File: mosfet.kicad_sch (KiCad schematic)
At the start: 4 parts

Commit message: v1
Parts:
- gave numbers to parts that had none: 4
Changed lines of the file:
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@@
 		(dnp no)
 		(fields_autoplaced yes)
-		(property "Reference" "#PWR032"
+		(property "Reference" "#PWR043"
 			(at 157.48 90.17 0)
 			(effects
@@
 			(project "aroma"
 				(path "/41d97073-34b5-4be3-afd3-c3d0ba6d78a9/41dcc568-047e-40c3-8917-993a0c1d8777"
-					(reference "#PWR042")
+					(reference "#PWR047")
 					(unit 1)
 				)
 				(path "/41d97073-34b5-4be3-afd3-c3d0ba6d78a9/5284dedf-81b9-4455-a1ae-4e68003b13db"
-					(reference "#PWR019")
+					(reference "#PWR045")
 					(unit 1)
 				)
 				(path "/41d97073-34b5-4be3-afd3-c3d0ba6d78a9/5e97d013-66fe-470c-accb-01dc7cf23fc6"
-					(reference "#PWR044")
+					(reference "#PWR049")
 					(unit 1)
 				)
 				(path "/41d97073-34b5-4be3-afd3-c3d0ba6d78a9/8980739a-e055-493d-bd80-b94c801de5e3"
-					(reference "#PWR032")
+					(reference "#PWR043")
 					(unit 1)
 				)
 				(path "/41d97073-34b5-4be3-afd3-c3d0ba6d78a9/b2304c8e-7f55-47b7-996b-0a7058ef6c5d"
-					(reference "#PWR049")
+					(reference "#PWR053")
 					(unit 1)
 				)
 				(path "/41d97073-34b5-4be3-afd3-c3d0ba6d78a9/fe386d5b-d6d2-4631-9499-27522be29692"
-					(reference "#PWR046")
+					(reference "#PWR051")
 					(unit 1)
 				)
@@
 		(dnp no)
 		(fields_autoplaced yes)
-		(property "Reference" "U?"
+		(property "Reference" "U8"
 			(at 134.62 90.17 0)
 			(effects
@@
 			(project "aroma"
 				(path "/41d97073-34b5-4be3-afd3-c3d0ba6d78a9/41dcc568-047e-40c3-8917-993a0c1d8777"
-					(reference "U?")
+					(reference "U10")
 					(unit 1)
 				)
 				(path "/41d97073-34b5-4be3-afd3-c3d0ba6d78a9/5284dedf-81b9-4455-a1ae-4e68003b13db"
-					(reference "U?")
+					(reference "U9")
 					(unit 1)
 				)
 				(path "/41d97073-34b5-4be3-afd3-c3d0ba6d78a9/5e97d013-66fe-470c-accb-01dc7cf23fc6"
-					(reference "U?")
+					(reference "U11")
 					(unit 1)
 				)
 				(path "/41d97073-34b5-4be3-afd3-c3d0ba6d78a9/8980739a-e055-493d-bd80-b94c801de5e3"
-					(reference "U?")
+					(reference "U8")
 					(unit 1)
 				)
 				(path "/41d97073-34b5-4be3-afd3-c3d0ba6d78a9/b2304c8e-7f55-47b7-996b-0a7058ef6c5d"
-					(reference "U?")
+					(reference "U13")
 					(unit 1)
 				)
 				(path "/41d97073-34b5-4be3-afd3-c3d0ba6d78a9/fe386d5b-d6d2-4631-9499-27522be29692"
-					(reference "U?")
+					(reference "U12")
 					(unit 1)
 				)
@@
 		(dnp no)
 		(fields_autoplaced yes)
-		(property "Reference" "R?"
+		(property "Reference" "R21"
 			(at 113.03 106.6799 0)
 			(effects
@@
 			(project "aroma"
 				(path "/41d97073-34b5-4be3-afd3-c3d0ba6d78a9/41dcc568-047e-40c3-8917-993a0c1d8777"
-					(reference "R?")
+					(reference "R23")
 					(unit 1)
 				)
 				(path "/41d97073-34b5-4be3-afd3-c3d0ba6d78a9/5284dedf-81b9-4455-a1ae-4e68003b13db"
-					(reference "R?")
+					(reference "R22")
 					(unit 1)
 				)
 				(path "/41d97073-34b5-4be3-afd3-c3d0ba6d78a9/5e97d013-66fe-470c-accb-01dc7cf23fc6"
-					(reference "R?")
+					(reference "R24")
 					(unit 1)
 				)
 				(path "/41d97073-34b5-4be3-afd3-c3d0ba6d78a9/8980739a-e055-493d-bd80-b94c801de5e3"
-					(reference "R?")
+					(reference "R21")
 					(unit 1)
 				)
 				(path "/41d97073-34b5-4be3-afd3-c3d0ba6d78a9/b2304c8e-7f55-47b7-996b-0a7058ef6c5d"
-					(reference "R?")
+					(reference "R26")
 					(unit 1)
 				)
 				(path "/41d97073-34b5-4be3-afd3-c3d0ba6d78a9/fe386d5b-d6d2-4631-9499-27522be29692"
-					(reference "R?")
+					(reference "R25")
 					(unit 1)
 				)
@@
 		(dnp no)
 		(fields_autoplaced yes)
-		(property "Reference" "J?"
+		(property "Reference" "J5"
 			(at 184.15 93.9799 0)
 			(effects
@@
 			(project "aroma"
 				(path "/41d97073-34b5-4be3-afd3-c3d0ba6d78a9/41dcc568-047e-40c3-8917-993a0c1d8777"
-					(reference "J?")
+					(reference "J7")
 					(unit 1)
 				)
 				(path "/41d97073-34b5-4be3-afd3-c3d0ba6d78a9/5284dedf-81b9-4455-a1ae-4e68003b13db"
-					(reference "J?")
+					(reference "J6")
 					(unit 1)
 				)
 				(path "/41d97073-34b5-4be3-afd3-c3d0ba6d78a9/5e97d013-66fe-470c-accb-01dc7cf23fc6"
-					(reference "J?")
+					(reference "J8")
 					(unit 1)
 				)
 				(path "/41d97073-34b5-4be3-afd3-c3d0ba6d78a9/8980739a-e055-493d-bd80-b94c801de5e3"
-					(reference "J?")
+					(reference "J5")
 					(unit 1)
 				)
 				(path "/41d97073-34b5-4be3-afd3-c3d0ba6d78a9/b2304c8e-7f55-47b7-996b-0a7058ef6c5d"
-					(reference "J?")
+					(reference "J10")
 					(unit 1)
 				)
 				(path "/41d97073-34b5-4be3-afd3-c3d0ba6d78a9/fe386d5b-d6d2-4631-9499-27522be29692"
-					(reference "J?")
+					(reference "J9")
 					(unit 1)
 				)
@@
 		(dnp no)
 		(fields_autoplaced yes)
-		(property "Reference" "#PWR047"
+		(property "Reference" "#PWR044"
 			(at 157.48 125.73 0)
 			(effects
@@
 			(project "aroma"
 				(path "/41d97073-34b5-4be3-afd3-c3d0ba6d78a9/41dcc568-047e-40c3-8917-993a0c1d8777"
-					(reference "#PWR043")
+					(reference "#PWR048")
 					(unit 1)
 				)
 				(path "/41d97073-34b5-4be3-afd3-c3d0ba6d78a9/5284dedf-81b9-4455-a1ae-4e68003b13db"
-					(reference "#PWR041")
+					(reference "#PWR046")
 					(unit 1)
 				)
 				(path "/41d97073-34b5-4be3-afd3-c3d0ba6d78a9/5e97d013-66fe-470c-accb-01dc7cf23fc6"
-					(reference "#PWR045")
+					(reference "#PWR050")
 					(unit 1)
 				)
 				(path "/41d97073-34b5-4be3-afd3-c3d0ba6d78a9/8980739a-e055-493d-bd80-b94c801de5e3"
-					(reference "#PWR047")
+					(reference "#PWR044")
 					(unit 1)
 				)
 				(path "/41d97073-34b5-4be3-afd3-c3d0ba6d78a9/b2304c8e-7f55-47b7-996b-0a7058ef6c5d"
-					(reference "#PWR050")
+					(reference "#PWR054")
 					(unit 1)
 				)
 				(path "/41d97073-34b5-4be3-afd3-c3d0ba6d78a9/fe386d5b-d6d2-4631-9499-27522be29692"
-					(reference "#PWR048")
+					(reference "#PWR052")
 					(unit 1)
 				)
@@
 		(dnp no)
 		(fields_autoplaced yes)
-		(property "Reference" "D?"
+		(property "Reference" "D5"
 			(at 160.02 93.6624 90)
 			(effects
@@
 			(project "aroma"
 				(path "/41d97073-34b5-4be3-afd3-c3d0ba6d78a9/41dcc568-047e-40c3-8917-993a0c1d8777"
-					(reference "D?")
+					(reference "D6")
 					(unit 1)
 				)
 				(path "/41d97073-34b5-4be3-afd3-c3d0ba6d78a9/5284dedf-81b9-4455-a1ae-4e68003b13db"
-					(reference "D?")
+					(reference "D5")
 					(unit 1)
 				)
 				(path "/41d97073-34b5-4be3-afd3-c3d0ba6d78a9/5e97d013-66fe-470c-accb-01dc7cf23fc6"
-					(reference "D?")
+					(reference "D7")
+					(unit 1)
+				)
+				(path "/41d97073-34b5-4be3-afd3-c3d0ba6d78a9/8980739a-e055-493d-bd80-b94c801de5e3"
+					(reference "D4")
 					(unit 1)
 				)
 				(path "/41d97073-34b5-4be3-afd3-c3d0ba6d78a9/b2304c8e-7f55-47b7-996b-0a7058ef6c5d"
-					(reference "D?")
+					(reference "D9")
 					(unit 1)
 				)
 				(path "/41d97073-34b5-4be3-afd3-c3d0ba6d78a9/fe386d5b-d6d2-4631-9499-27522be29692"
-					(reference "D?")
-					(unit 1)
-				)
+					(reference "D8")
+					(unit 1)
+				)

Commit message: v2
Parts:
- renumbered D5 to D6, J5 to J7, R21 to R23, U8 to U6
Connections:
- net +5V: now also J7.2; no longer J7.1
- net at D6.2 (A), U6.3: now also J7.1; no longer J7.2
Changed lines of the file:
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@@
 		(dnp no)
 		(fields_autoplaced yes)
-		(property "Reference" "#PWR043"
+		(property "Reference" "#PWR049"
 			(at 157.48 90.17 0)
 			(effects
@@
 			(project "aroma"
 				(path "/41d97073-34b5-4be3-afd3-c3d0ba6d78a9/41dcc568-047e-40c3-8917-993a0c1d8777"
+					(reference "#PWR049")
+					(unit 1)
+				)
+				(path "/41d97073-34b5-4be3-afd3-c3d0ba6d78a9/5284dedf-81b9-4455-a1ae-4e68003b13db"
 					(reference "#PWR047")
 					(unit 1)
 				)
-				(path "/41d97073-34b5-4be3-afd3-c3d0ba6d78a9/5284dedf-81b9-4455-a1ae-4e68003b13db"
+				(path "/41d97073-34b5-4be3-afd3-c3d0ba6d78a9/5e97d013-66fe-470c-accb-01dc7cf23fc6"
+					(reference "#PWR051")
+					(unit 1)
+				)
+				(path "/41d97073-34b5-4be3-afd3-c3d0ba6d78a9/8980739a-e055-493d-bd80-b94c801de5e3"
 					(reference "#PWR045")
 					(unit 1)
 				)
-				(path "/41d97073-34b5-4be3-afd3-c3d0ba6d78a9/5e97d013-66fe-470c-accb-01dc7cf23fc6"
-					(reference "#PWR049")
-					(unit 1)
-				)
-				(path "/41d97073-34b5-4be3-afd3-c3d0ba6d78a9/8980739a-e055-493d-bd80-b94c801de5e3"
-					(reference "#PWR043")
-					(unit 1)
-				)
 				(path "/41d97073-34b5-4be3-afd3-c3d0ba6d78a9/b2304c8e-7f55-47b7-996b-0a7058ef6c5d"
+					(reference "#PWR055")
+					(unit 1)
+				)
+				(path "/41d97073-34b5-4be3-afd3-c3d0ba6d78a9/fe386d5b-d6d2-4631-9499-27522be29692"
 					(reference "#PWR053")
-					(unit 1)
-				)
-				(path "/41d97073-34b5-4be3-afd3-c3d0ba6d78a9/fe386d5b-d6d2-4631-9499-27522be29692"
-					(reference "#PWR051")
 					(unit 1)
 				)
@@
 		(dnp no)
 		(fields_autoplaced yes)
-		(property "Reference" "U8"
+		(property "Reference" "U6"
 			(at 134.62 90.17 0)
 			(effects
@@
 			(project "aroma"
 				(path "/41d97073-34b5-4be3-afd3-c3d0ba6d78a9/41dcc568-047e-40c3-8917-993a0c1d8777"
-					(reference "U10")
+					(reference "U6")
 					(unit 1)
 				)
 				(path "/41d97073-34b5-4be3-afd3-c3d0ba6d78a9/5284dedf-81b9-4455-a1ae-4e68003b13db"
+					(reference "U5")
+					(unit 1)
+				)
+				(path "/41d97073-34b5-4be3-afd3-c3d0ba6d78a9/5e97d013-66fe-470c-accb-01dc7cf23fc6"
+					(reference "U7")
+					(unit 1)
+				)
+				(path "/41d97073-34b5-4be3-afd3-c3d0ba6d78a9/8980739a-e055-493d-bd80-b94c801de5e3"
+					(reference "U4")
+					(unit 1)
+				)
+				(path "/41d97073-34b5-4be3-afd3-c3d0ba6d78a9/b2304c8e-7f55-47b7-996b-0a7058ef6c5d"
 					(reference "U9")
 					(unit 1)
 				)
-				(path "/41d97073-34b5-4be3-afd3-c3d0ba6d78a9/5e97d013-66fe-470c-accb-01dc7cf23fc6"
-					(reference "U11")
-					(unit 1)
-				)
-				(path "/41d97073-34b5-4be3-afd3-c3d0ba6d78a9/8980739a-e055-493d-bd80-b94c801de5e3"
+				(path "/41d97073-34b5-4be3-afd3-c3d0ba6d78a9/fe386d5b-d6d2-4631-9499-27522be29692"
 					(reference "U8")
-					(unit 1)
-				)
-				(path "/41d97073-34b5-4be3-afd3-c3d0ba6d78a9/b2304c8e-7f55-47b7-996b-0a7058ef6c5d"
-					(reference "U13")
-					(unit 1)
-				)
-				(path "/41d97073-34b5-4be3-afd3-c3d0ba6d78a9/fe386d5b-d6d2-4631-9499-27522be29692"
-					(reference "U12")
 					(unit 1)
 				)
@@
 		(dnp no)
 		(fields_autoplaced yes)
-		(property "Reference" "R21"
+		(property "Reference" "R23"
 			(at 113.03 106.6799 0)
 			(effects
@@
 	(symbol
 		(lib_id "2pinmolex:2157601002")
-		(at 170.18 93.98 0)
+		(at 170.18 96.52 0)
+		(mirror x)
 		(unit 1)
 		(exclude_from_sim no)
@@
 		(on_board yes)
 		(dnp no)
-		(fields_autoplaced yes)
-		(property "Reference" "J5"
-			(at 184.15 93.9799 0)
+		(property "Reference" "J7"
+			(at 184.15 96.5201 0)
 			(effects
 				(font
@@
 		)
 		(property "Value" "2157601002"
-			(at 184.15 96.5199 0)
+			(at 184.15 93.9801 0)
 			(effects
 				(font
@@
 		)
 		(property "Footprint" "CONN02_2157601002_MOL"
-			(at 170.18 93.98 0)
+			(at 170.18 96.52 0)
 			(effects
 				(font
@@
 		)
 		(property "Datasheet" "2157601002"
-			(at 170.18 93.98 0)
+			(at 170.18 96.52 0)
 			(effects
 				(font
@@
 		)
 		(property "Description" ""
-			(at 170.18 93.98 0)
+			(at 170.18 96.52 0)
 			(effects
 				(font
@@
 		(dnp no)
 		(fields_autoplaced yes)
-		(property "Reference" "#PWR044"
+		(property "Reference" "#PWR050"
 			(at 157.48 125.73 0)
 			(effects
@@
 			(project "aroma"
 				(path "/41d97073-34b5-4be3-afd3-c3d0ba6d78a9/41dcc568-047e-40c3-8917-993a0c1d8777"
+					(reference "#PWR050")
+					(unit 1)
+				)
+				(path "/41d97073-34b5-4be3-afd3-c3d0ba6d78a9/5284dedf-81b9-4455-a1ae-4e68003b13db"
 					(reference "#PWR048")
 					(unit 1)
 				)
-				(path "/41d97073-34b5-4be3-afd3-c3d0ba6d78a9/5284dedf-81b9-4455-a1ae-4e68003b13db"
+				(path "/41d97073-34b5-4be3-afd3-c3d0ba6d78a9/5e97d013-66fe-470c-accb-01dc7cf23fc6"
+					(reference "#PWR052")
+					(unit 1)
+				)
+				(path "/41d97073-34b5-4be3-afd3-c3d0ba6d78a9/8980739a-e055-493d-bd80-b94c801de5e3"
 					(reference "#PWR046")
 					(unit 1)
 				)
-				(path "/41d97073-34b5-4be3-afd3-c3d0ba6d78a9/5e97d013-66fe-470c-accb-01dc7cf23fc6"
-					(reference "#PWR050")
-					(unit 1)
-				)
-				(path "/41d97073-34b5-4be3-afd3-c3d0ba6d78a9/8980739a-e055-493d-bd80-b94c801de5e3"
-					(reference "#PWR044")
-					(unit 1)
-				)
 				(path "/41d97073-34b5-4be3-afd3-c3d0ba6d78a9/b2304c8e-7f55-47b7-996b-0a7058ef6c5d"
+					(reference "#PWR056")
+					(unit 1)
+				)
+				(path "/41d97073-34b5-4be3-afd3-c3d0ba6d78a9/fe386d5b-d6d2-4631-9499-27522be29692"
 					(reference "#PWR054")
-					(unit 1)
-				)
-				(path "/41d97073-34b5-4be3-afd3-c3d0ba6d78a9/fe386d5b-d6d2-4631-9499-27522be29692"
-					(reference "#PWR052")
 					(unit 1)
 				)
@@
 		(dnp no)
 		(fields_autoplaced yes)
-		(property "Reference" "D5"
+		(property "Reference" "D6"
 			(at 160.02 93.6624 90)
 			(effects

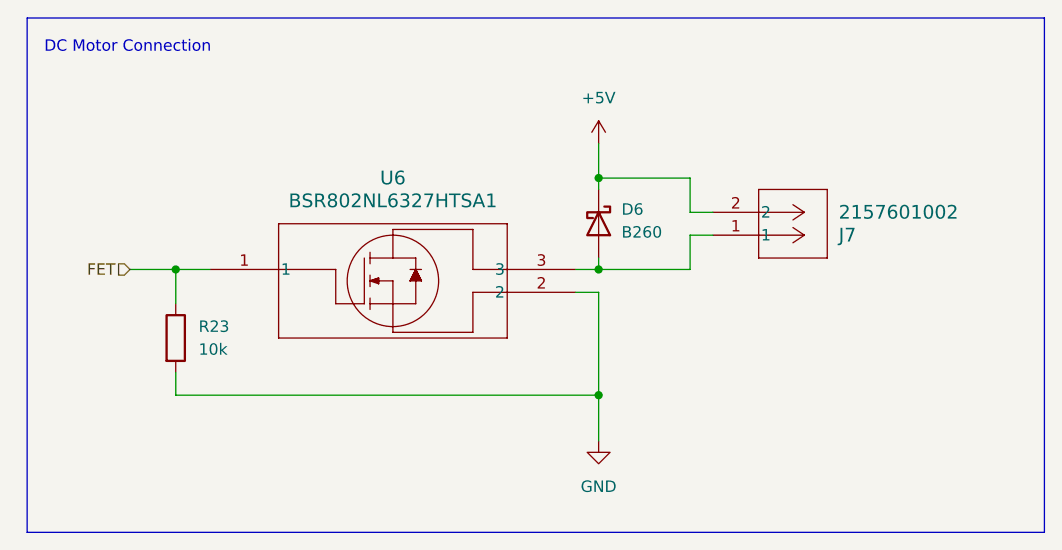
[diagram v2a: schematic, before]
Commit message: LCD Display
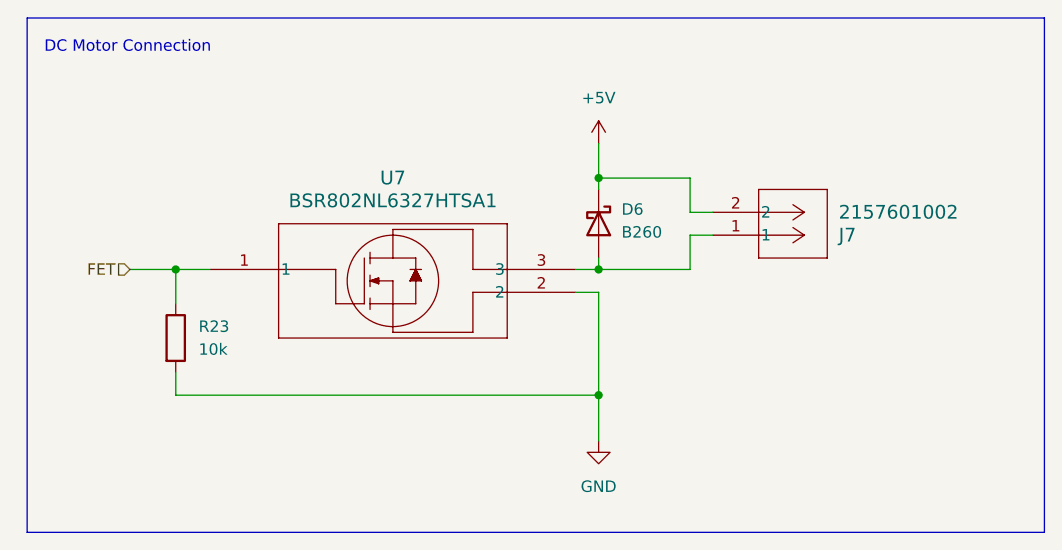
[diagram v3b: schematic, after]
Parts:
- renumbered U6 to U7
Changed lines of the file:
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@@
 		(dnp no)
 		(fields_autoplaced yes)
-		(property "Reference" "#PWR049"
+		(property "Reference" "#PWR051"
 			(at 157.48 90.17 0)
 			(effects
@@
 			(project "aroma"
 				(path "/41d97073-34b5-4be3-afd3-c3d0ba6d78a9/41dcc568-047e-40c3-8917-993a0c1d8777"
+					(reference "#PWR051")
+					(unit 1)
+				)
+				(path "/41d97073-34b5-4be3-afd3-c3d0ba6d78a9/5284dedf-81b9-4455-a1ae-4e68003b13db"
 					(reference "#PWR049")
 					(unit 1)
 				)
-				(path "/41d97073-34b5-4be3-afd3-c3d0ba6d78a9/5284dedf-81b9-4455-a1ae-4e68003b13db"
+				(path "/41d97073-34b5-4be3-afd3-c3d0ba6d78a9/5e97d013-66fe-470c-accb-01dc7cf23fc6"
+					(reference "#PWR053")
+					(unit 1)
+				)
+				(path "/41d97073-34b5-4be3-afd3-c3d0ba6d78a9/8980739a-e055-493d-bd80-b94c801de5e3"
 					(reference "#PWR047")
 					(unit 1)
 				)
-				(path "/41d97073-34b5-4be3-afd3-c3d0ba6d78a9/5e97d013-66fe-470c-accb-01dc7cf23fc6"
-					(reference "#PWR051")
-					(unit 1)
-				)
-				(path "/41d97073-34b5-4be3-afd3-c3d0ba6d78a9/8980739a-e055-493d-bd80-b94c801de5e3"
-					(reference "#PWR045")
-					(unit 1)
-				)
 				(path "/41d97073-34b5-4be3-afd3-c3d0ba6d78a9/b2304c8e-7f55-47b7-996b-0a7058ef6c5d"
+					(reference "#PWR057")
+					(unit 1)
+				)
+				(path "/41d97073-34b5-4be3-afd3-c3d0ba6d78a9/fe386d5b-d6d2-4631-9499-27522be29692"
 					(reference "#PWR055")
-					(unit 1)
-				)
-				(path "/41d97073-34b5-4be3-afd3-c3d0ba6d78a9/fe386d5b-d6d2-4631-9499-27522be29692"
-					(reference "#PWR053")
 					(unit 1)
 				)
@@
 		(dnp no)
 		(fields_autoplaced yes)
-		(property "Reference" "U6"
+		(property "Reference" "U7"
 			(at 134.62 90.17 0)
 			(effects
@@
 			(project "aroma"
 				(path "/41d97073-34b5-4be3-afd3-c3d0ba6d78a9/41dcc568-047e-40c3-8917-993a0c1d8777"
+					(reference "U7")
+					(unit 1)
+				)
+				(path "/41d97073-34b5-4be3-afd3-c3d0ba6d78a9/5284dedf-81b9-4455-a1ae-4e68003b13db"
 					(reference "U6")
 					(unit 1)
 				)
-				(path "/41d97073-34b5-4be3-afd3-c3d0ba6d78a9/5284dedf-81b9-4455-a1ae-4e68003b13db"
+				(path "/41d97073-34b5-4be3-afd3-c3d0ba6d78a9/5e97d013-66fe-470c-accb-01dc7cf23fc6"
+					(reference "U8")
+					(unit 1)
+				)
+				(path "/41d97073-34b5-4be3-afd3-c3d0ba6d78a9/8980739a-e055-493d-bd80-b94c801de5e3"
 					(reference "U5")
 					(unit 1)
 				)
-				(path "/41d97073-34b5-4be3-afd3-c3d0ba6d78a9/5e97d013-66fe-470c-accb-01dc7cf23fc6"
-					(reference "U7")
-					(unit 1)
-				)
-				(path "/41d97073-34b5-4be3-afd3-c3d0ba6d78a9/8980739a-e055-493d-bd80-b94c801de5e3"
-					(reference "U4")
-					(unit 1)
-				)
 				(path "/41d97073-34b5-4be3-afd3-c3d0ba6d78a9/b2304c8e-7f55-47b7-996b-0a7058ef6c5d"
+					(reference "U10")
+					(unit 1)
+				)
+				(path "/41d97073-34b5-4be3-afd3-c3d0ba6d78a9/fe386d5b-d6d2-4631-9499-27522be29692"
 					(reference "U9")
-					(unit 1)
-				)
-				(path "/41d97073-34b5-4be3-afd3-c3d0ba6d78a9/fe386d5b-d6d2-4631-9499-27522be29692"
-					(reference "U8")
 					(unit 1)
 				)
@@
 		(dnp no)
 		(fields_autoplaced yes)
-		(property "Reference" "#PWR050"
+		(property "Reference" "#PWR052"
 			(at 157.48 125.73 0)
 			(effects
@@
 			(project "aroma"
 				(path "/41d97073-34b5-4be3-afd3-c3d0ba6d78a9/41dcc568-047e-40c3-8917-993a0c1d8777"
+					(reference "#PWR052")
+					(unit 1)
+				)
+				(path "/41d97073-34b5-4be3-afd3-c3d0ba6d78a9/5284dedf-81b9-4455-a1ae-4e68003b13db"
 					(reference "#PWR050")
 					(unit 1)
 				)
-				(path "/41d97073-34b5-4be3-afd3-c3d0ba6d78a9/5284dedf-81b9-4455-a1ae-4e68003b13db"
+				(path "/41d97073-34b5-4be3-afd3-c3d0ba6d78a9/5e97d013-66fe-470c-accb-01dc7cf23fc6"
+					(reference "#PWR054")
+					(unit 1)
+				)
+				(path "/41d97073-34b5-4be3-afd3-c3d0ba6d78a9/8980739a-e055-493d-bd80-b94c801de5e3"
 					(reference "#PWR048")
 					(unit 1)
 				)
-				(path "/41d97073-34b5-4be3-afd3-c3d0ba6d78a9/5e97d013-66fe-470c-accb-01dc7cf23fc6"
-					(reference "#PWR052")
-					(unit 1)
-				)
-				(path "/41d97073-34b5-4be3-afd3-c3d0ba6d78a9/8980739a-e055-493d-bd80-b94c801de5e3"
-					(reference "#PWR046")
-					(unit 1)
-				)
 				(path "/41d97073-34b5-4be3-afd3-c3d0ba6d78a9/b2304c8e-7f55-47b7-996b-0a7058ef6c5d"
+					(reference "#PWR058")
+					(unit 1)
+				)
+				(path "/41d97073-34b5-4be3-afd3-c3d0ba6d78a9/fe386d5b-d6d2-4631-9499-27522be29692"
 					(reference "#PWR056")
 					(unit 1)
 				)
-				(path "/41d97073-34b5-4be3-afd3-c3d0ba6d78a9/fe386d5b-d6d2-4631-9499-27522be29692"
-					(reference "#PWR054")
-					(unit 1)
-				)
